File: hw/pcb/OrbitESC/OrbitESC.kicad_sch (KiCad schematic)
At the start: 0 parts

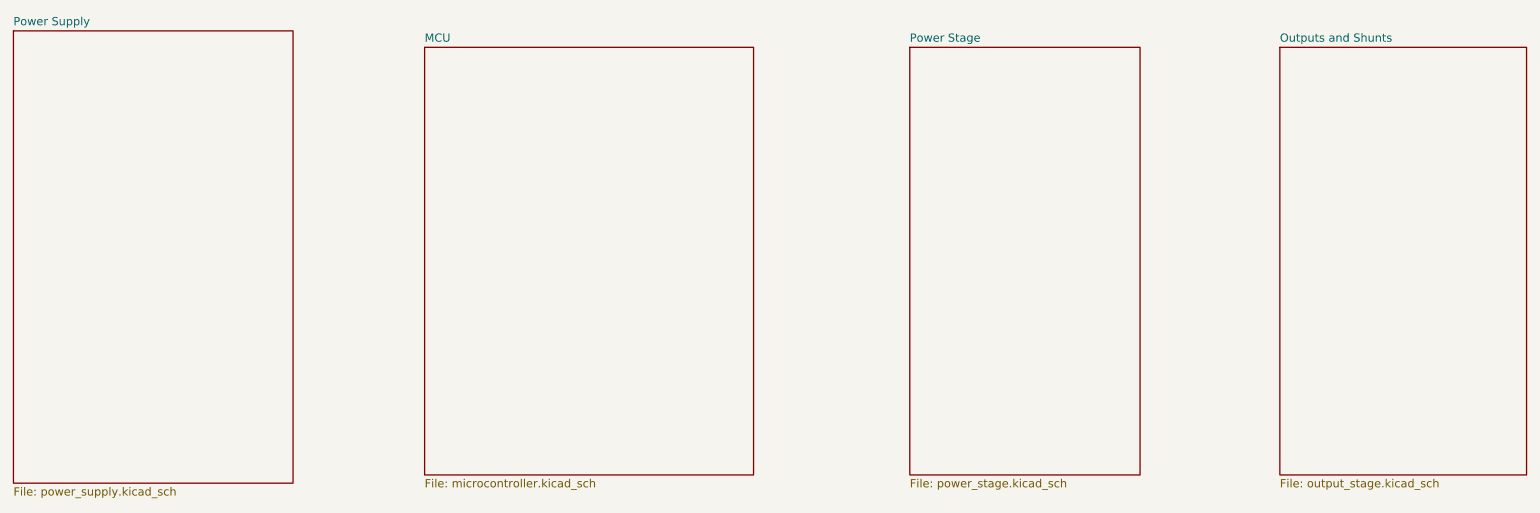
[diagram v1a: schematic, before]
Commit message: Add power stage components
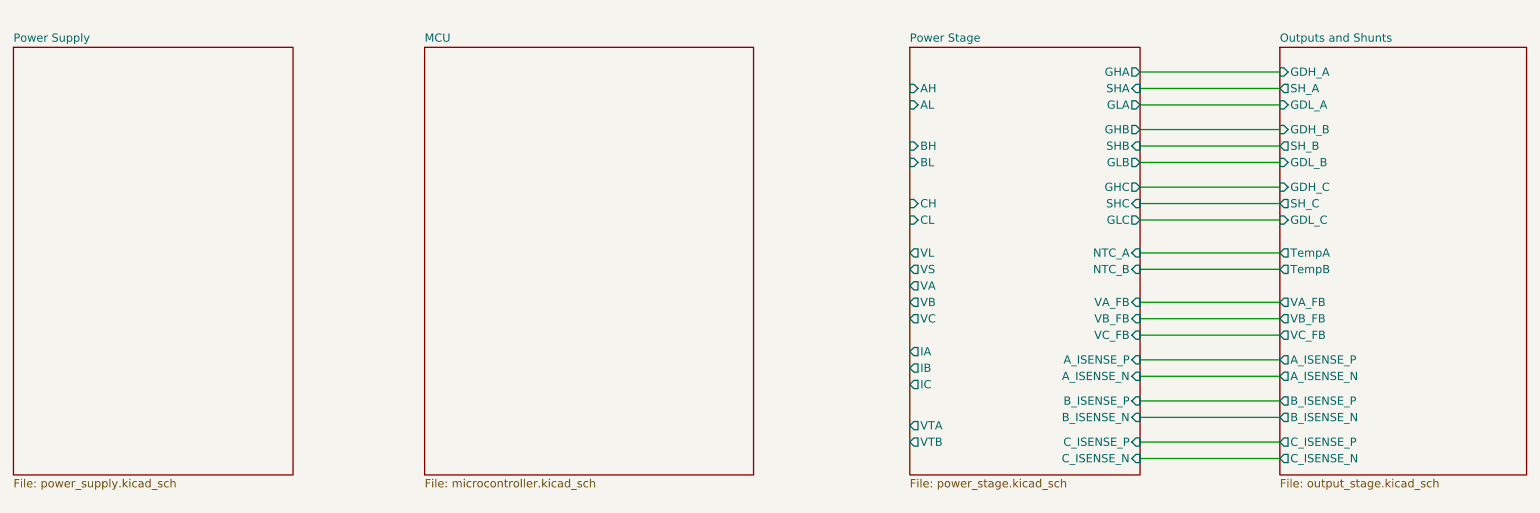
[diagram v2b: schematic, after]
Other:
- sheet Outputs and Shunts ports: added A_ISENSE_N, A_ISENSE_P, B_ISENSE_N, B_ISENSE_P, C_ISENSE_N, C_ISENSE_P, GDH_A, GDH_B, GDH_C, GDL_A, GDL_B, GDL_C, SH_A, SH_B, SH_C, TempA, TempB, VA_FB, VB_FB, VC_FB; removed none
- sheet Power Stage ports: added AH, AL, A_ISENSE_N, A_ISENSE_P, BH, BL, B_ISENSE_N, B_ISENSE_P, CH, CL, C_ISENSE_N, C_ISENSE_P, GHA, GHB, GHC, GLA, GLB, GLC, IA, IB, IC, NTC_A, NTC_B, SHA, SHB, SHC, VA, VA_FB, VB, VB_FB, VC, VC_FB, VL, VS, VTA, VTB; removed none

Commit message: Initial planning of MCU connections
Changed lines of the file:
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@@
       (effects (font (size 1.27 1.27)) (justify left))
     )
-    (pin "VC" output (at 163.83 88.9 180)
+    (pin "VC" output (at 163.83 86.36 180)
       (effects (font (size 1.27 1.27)) (justify left))
     )
@@
       (effects (font (size 1.27 1.27)) (justify left))
     )
-    (pin "VS" output (at 163.83 81.28 180)
-      (effects (font (size 1.27 1.27)) (justify left))
-    )
-    (pin "VB" output (at 163.83 86.36 180)
+    (pin "VS" output (at 163.83 91.44 180)
+      (effects (font (size 1.27 1.27)) (justify left))
+    )
+    (pin "VB" output (at 163.83 83.82 180)
       (effects (font (size 1.27 1.27)) (justify left))
     )
@@
       (effects (font (size 1.27 1.27)) (justify left))
     )
-    (pin "VA" output (at 163.83 83.82 180)
+    (pin "VA" output (at 163.83 81.28 180)
       (effects (font (size 1.27 1.27)) (justify left))
     )
@@
       (effects (font (size 1.27 1.27)) (justify left))
     )
-    (pin "VL" output (at 163.83 78.74 180)
+    (pin "VL" output (at 163.83 110.49 180)
       (effects (font (size 1.27 1.27)) (justify left))
     )
@@
     )
     (path "/ed067bb8-caa7-448e-917b-cc2d33c8b4b7/0efcfcef-7bcd-4cdd-8030-cd7584ba0000"
-      (reference "#PWR?") (unit 1) (value "+5V") (footprint "")
+      (reference "#PWR038") (unit 1) (value "+5V") (footprint "")
+    )
+    (path "/ed067bb8-caa7-448e-917b-cc2d33c8b4b7/d46610f9-5ec7-4597-a350-2c4dab734b37"
+      (reference "#PWR039") (unit 1) (value "+3.3VADC") (footprint "")
+    )
+    (path "/ed067bb8-caa7-448e-917b-cc2d33c8b4b7/c15c4b35-7a6a-4fcb-b46b-7f05553f64d4"
+      (reference "#PWR040") (unit 1) (value "VBUS") (footprint "")
     )
     (path "/ed067bb8-caa7-448e-917b-cc2d33c8b4b7/2f017ece-9ff4-409b-9c32-6e3116c0e01b"
-      (reference "#PWR?") (unit 1) (value "+3.3V") (footprint "")
-    )
-    (path "/ed067bb8-caa7-448e-917b-cc2d33c8b4b7/c15c4b35-7a6a-4fcb-b46b-7f05553f64d4"
-      (reference "#PWR?") (unit 1) (value "VBUS") (footprint "")
-    )
-    (path "/ed067bb8-caa7-448e-917b-cc2d33c8b4b7/d46610f9-5ec7-4597-a350-2c4dab734b37"
-      (reference "#PWR?") (unit 1) (value "+3.3VADC") (footprint "")
+      (reference "#PWR041") (unit 1) (value "+3.3V") (footprint "")
     )
     (path "/01eceaba-0372-470e-b19c-b8e61f77bd53/f2efe7d0-4630-49c1-9621-c2f0af362af3"
@@
     )
     (path "/ed067bb8-caa7-448e-917b-cc2d33c8b4b7/30a0b438-c213-480f-96f4-886bd88088c6"
-      (reference "D?") (unit 1) (value "Blue LED") (footprint "Diode_SMD:D_0603_1608Metric")
+      (reference "D5") (unit 1) (value "Blue LED") (footprint "Diode_SMD:D_0603_1608Metric")
     )
     (path "/e5c7e094-5305-4041-9a38-3256d4457e28/a3640a4b-0f7f-414c-8cb2-416ea2b405c5"
@@
     )
     (path "/ed067bb8-caa7-448e-917b-cc2d33c8b4b7/df5f7361-2f8e-4212-b013-59e810112187"
-      (reference "R?") (unit 1) (value "200") (footprint "Resistor_SMD:R_0402_1005Metric")
+      (reference "R47") (unit 1) (value "200") (footprint "Resistor_SMD:R_0402_1005Metric")
+    )
+    (path "/ed067bb8-caa7-448e-917b-cc2d33c8b4b7/1624da69-3900-4f5f-85af-9b1cb94d2c48"
+      (reference "SW?") (unit 1) (value "Break") (footprint "Button_Switch_SMD:SW_SPST_PTS810")
+    )
+    (path "/ed067bb8-caa7-448e-917b-cc2d33c8b4b7/df4ed6f6-4e7a-4da6-ab28-54c5e3335ad3"
+      (reference "SW?") (unit 1) (value "Boot") (footprint "Button_Switch_SMD:SW_SPST_PTS810")
+    )
+    (path "/ed067bb8-caa7-448e-917b-cc2d33c8b4b7/fe777dc0-c7bb-43f4-b858-2861285291be"
+      (reference "SW?") (unit 1) (value "Reset") (footprint "Button_Switch_SMD:SW_SPST_PTS810")
     )
     (path "/01eceaba-0372-470e-b19c-b8e61f77bd53/822ba713-bed0-4bf2-9c55-db2be437b8bc"

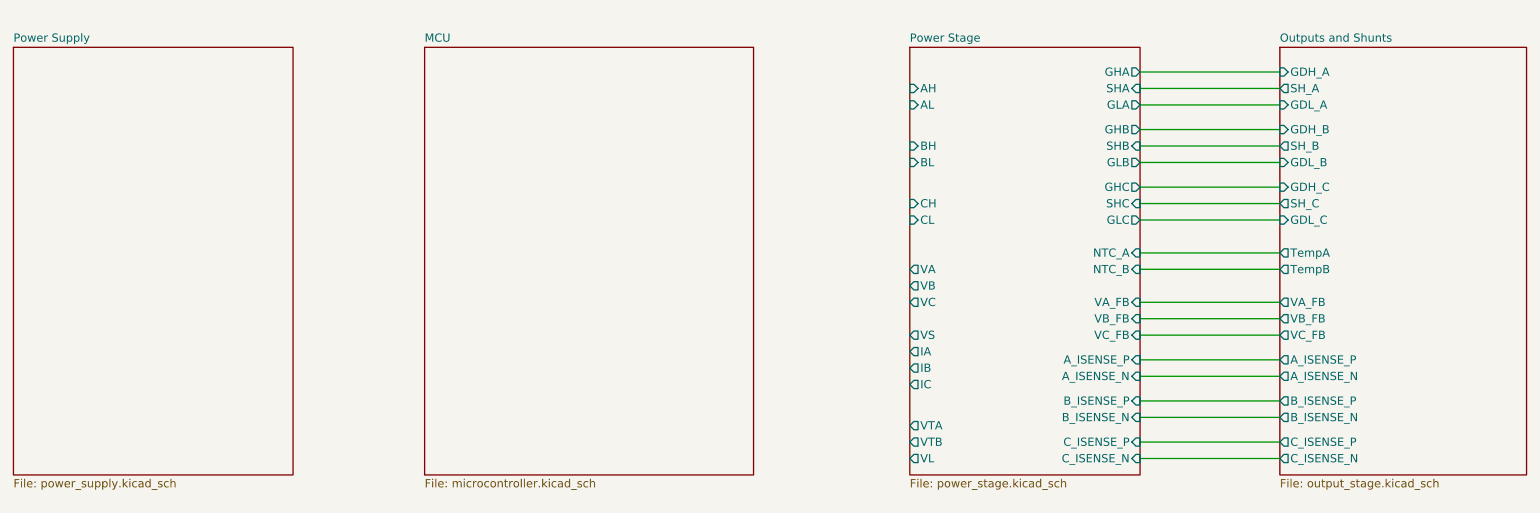
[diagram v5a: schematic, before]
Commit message: Fill out majority of schematic
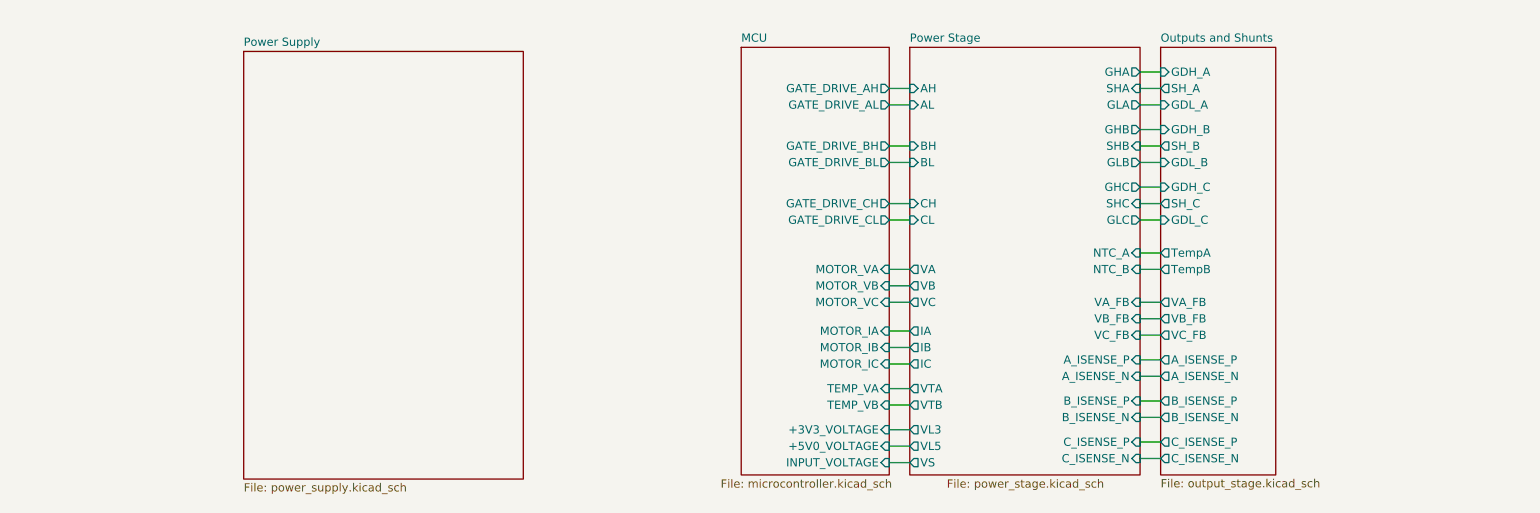
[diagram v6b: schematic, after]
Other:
- sheet MCU ports: added +3V3_VOLTAGE, +5V0_VOLTAGE, GATE_DRIVE_AH, GATE_DRIVE_AL, GATE_DRIVE_BH, GATE_DRIVE_BL, GATE_DRIVE_CH, GATE_DRIVE_CL, INPUT_VOLTAGE, MOTOR_IA, MOTOR_IB, MOTOR_IC, MOTOR_VA, MOTOR_VB, MOTOR_VC, TEMP_VA, TEMP_VB; removed none
- sheet Power Stage ports: added VL3, VL5; removed VL
